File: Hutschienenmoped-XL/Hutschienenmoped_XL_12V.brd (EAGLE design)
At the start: 96.3 x 101.8 mm, 119 parts, among them J1 638207222005, J13 638207222005, J15 638207222008, J2 645004114822, J4 61300421121, J7 638207222005, J8 638207222007, U4 TLE9250VSJ

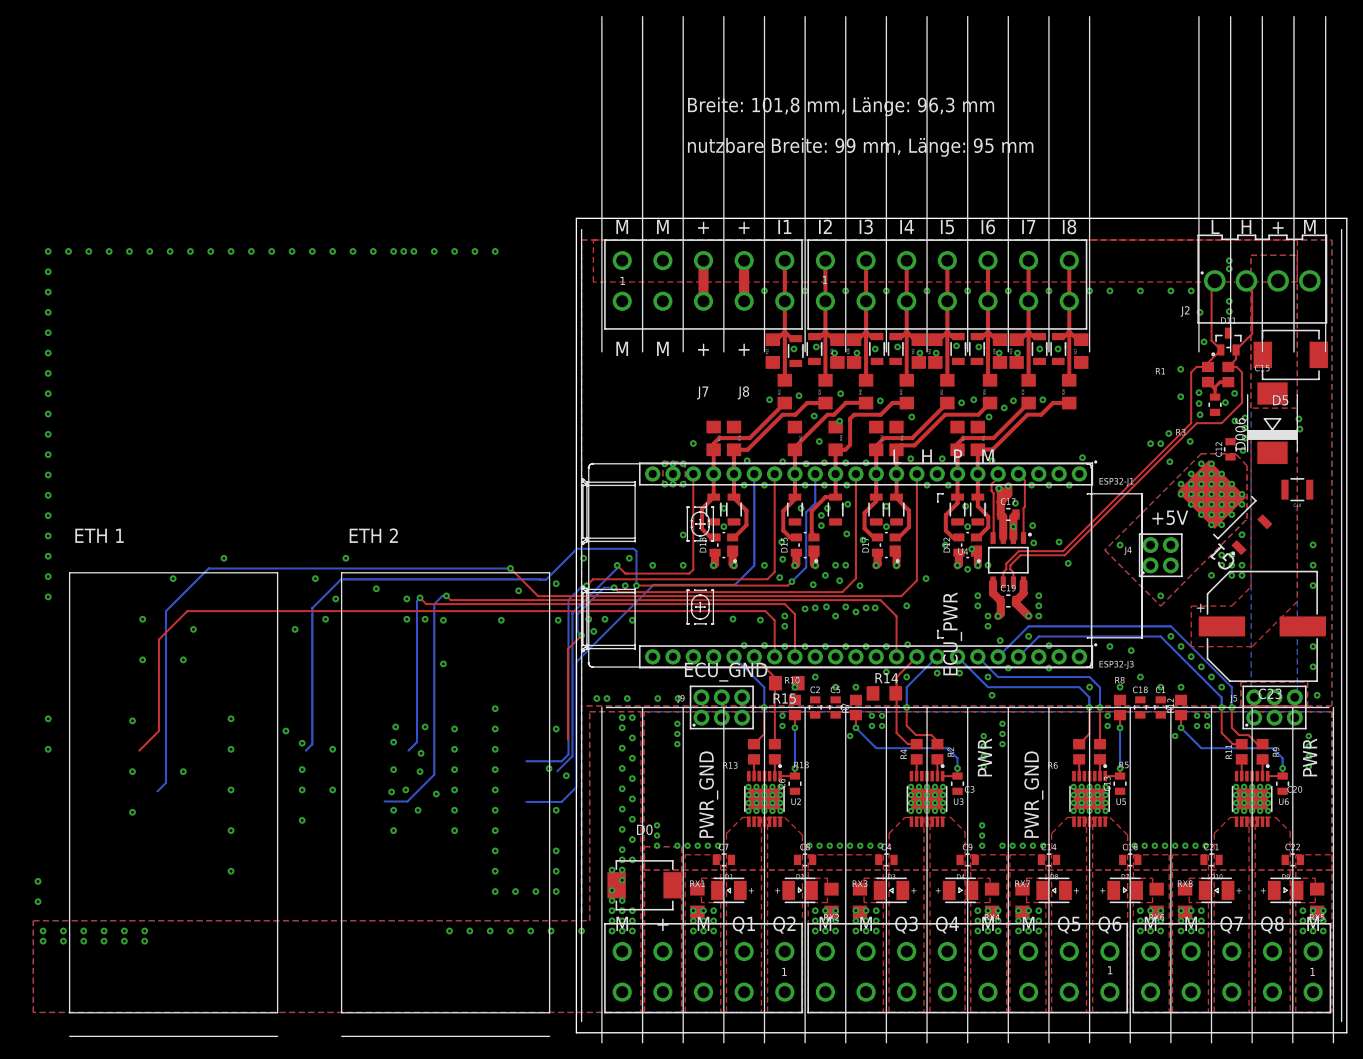
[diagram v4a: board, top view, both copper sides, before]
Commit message: Update grid settings and Fusion 360 sync details, remove redundant wires and text elements, optimize polygon vertices, clean up vias and wire connections.
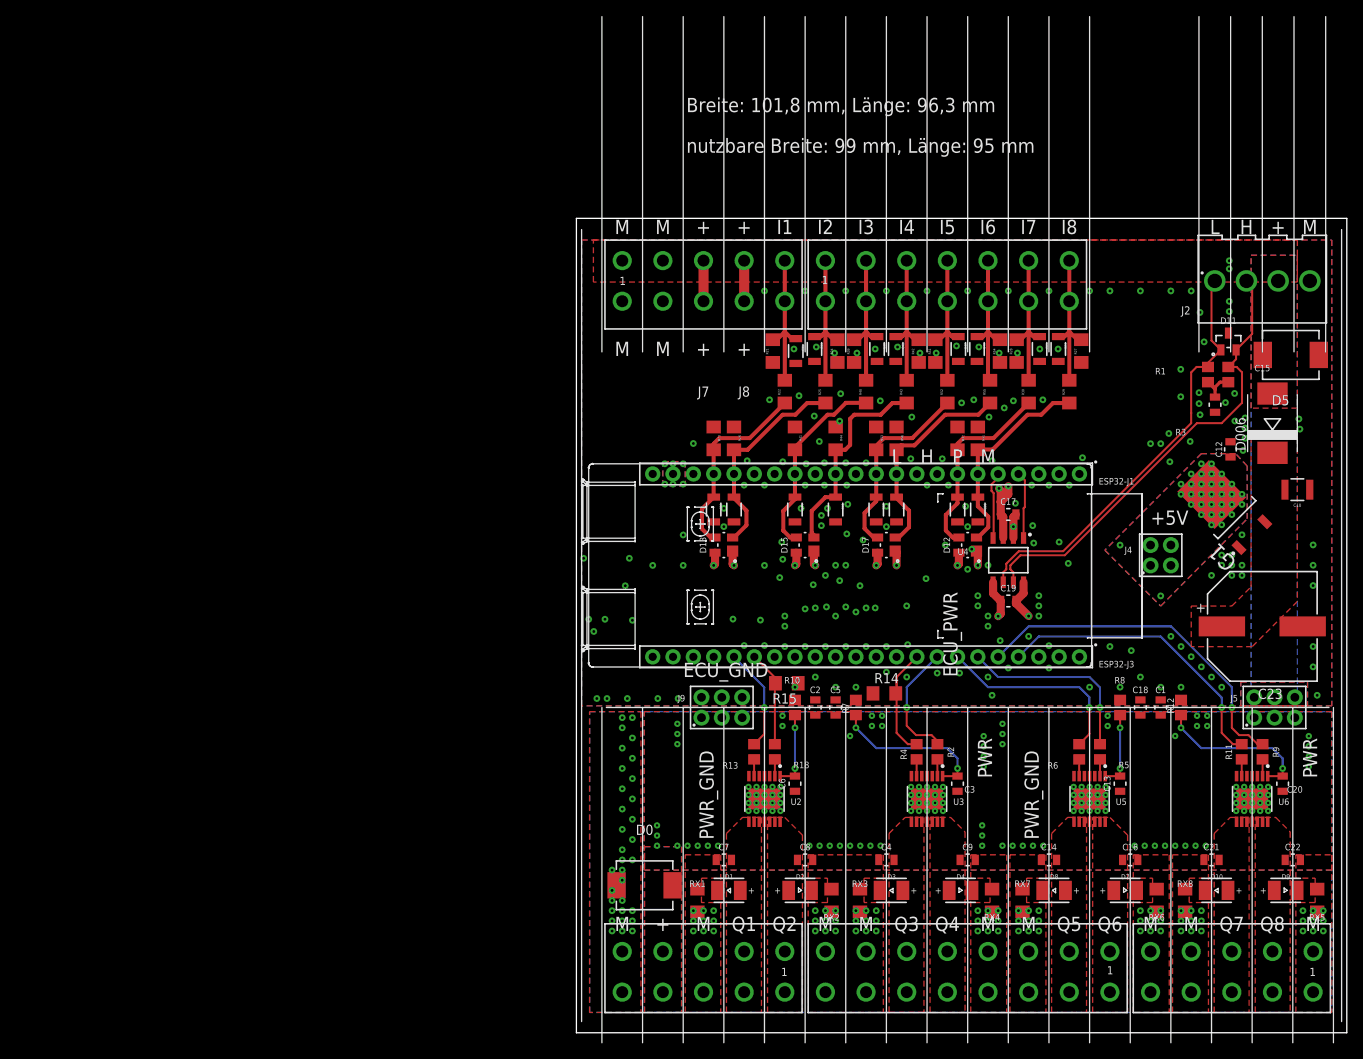
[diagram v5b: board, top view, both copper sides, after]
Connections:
- removed net CS0: ESP32-J1.14
- removed net CS1: ESP32-J1.12
- removed net INT0: ESP32-J3.16
- removed net INT1: ESP32-J3.15
- removed net MISO: ESP32-J1.20
- removed net MOSI: ESP32-J1.17
- removed net RST0: ESP32-J1.9
- removed net RST1: ESP32-J3.10
- removed net SCLK: ESP32-J1.16
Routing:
- net RST0: track 134.6 -> 0.00 mm, vias 1 -> 0
- net CS0: track 100.5 -> 0.00 mm, vias 2 -> 0
- net INT0: track 98.4 -> 0.00 mm
- net RST1: track 93.3 -> 0.00 mm, vias 1 -> 0
- net INT1: track 72.7 -> 0.00 mm, vias 1 -> 0
- net CS1: track 66.8 -> 0.00 mm, vias 2 -> 0
- net SCLK: track 64.4 -> 0.00 mm, vias 1 -> 0
- net MOSI: track 61.3 -> 0.00 mm
- net MISO: track 50.9 -> 0.00 mm, vias 1 -> 0
- net ECU_GND: vias 333 -> 214
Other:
- board text removed: "ETH 1"
- board text removed: "ETH 2"
